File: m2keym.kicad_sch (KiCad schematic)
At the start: 14 parts, among them J6 Bus_M.2_1-2199230-6

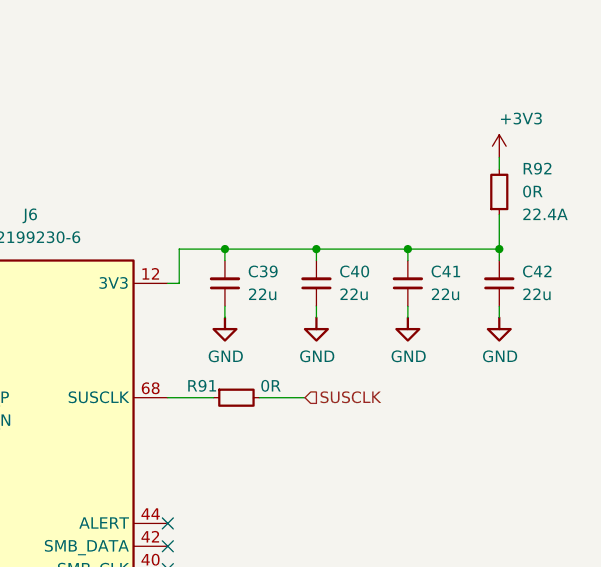
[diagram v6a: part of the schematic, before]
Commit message: [#58137] Add DC/DC supplies
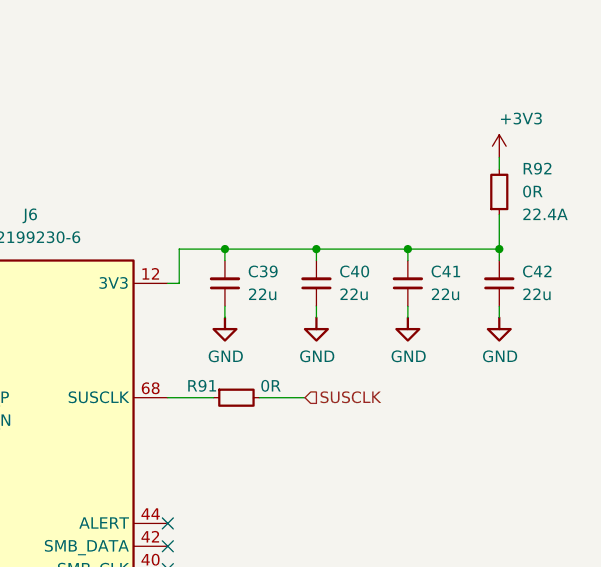
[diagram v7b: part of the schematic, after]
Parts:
- C39, C40, C41, C42: value C_22u_0603 -> C_22u_16V_0603; symbol antmicroCapacitors0603:C_22u_0603 -> antmicroCapacitors0603:C_22u_16V_0603; MPN GRM188R60J226MEA0D -> CL10A226MO7JZNC; Manufacturer Murata -> Samsung Electro-Mechanics; Voltage (none) -> 16V
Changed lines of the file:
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@@
     )
   )
-  (symbol (lib_id "antmicroCapacitors0603:C_22u_0603") (at 267.97 91.44 90) (unit 1)
+  (symbol (lib_id "antmicroCapacitors0603:C_22u_16V_0603") (at 267.97 91.44 90) (unit 1)
     (in_bom yes) (on_board yes) (dnp no) (fields_autoplaced)
-    (property "Reference" "C42" (at 270.51 87.6236 90)
-      (effects (font (size 1.27 1.27) (thickness 0.15)) (justify right))
-    )
-    (property "Value" "C_22u_0603" (at 278.13 71.12 0)
+    (property "Reference" "C42" (at 270.51 87.6235 90)
+      (effects (font (size 1.27 1.27) (thickness 0.15)) (justify right))
+    )
+    (property "Value" "C_22u_16V_0603" (at 278.13 71.12 0)
       (effects (font (size 1.27 1.27) (thickness 0.15)) (justify left bottom) hide)
     )
@@
       (effects (font (size 1.27 1.27) (thickness 0.15)) (justify left bottom) hide)
     )
-    (property "Datasheet" "https://www.murata.com/products/productdetail?partno=GRM188R60J226MEA0%23" (at 283.21 71.12 0)
-      (effects (font (size 1.27 1.27) (thickness 0.15)) (justify left bottom) hide)
-    )
-    (property "MPN" "GRM188R60J226MEA0D" (at 285.75 71.12 0)
-      (effects (font (size 1.27 1.27) (thickness 0.15)) (justify left bottom) hide)
-    )
-    (property "Manufacturer" "Murata" (at 288.29 71.12 0)
+    (property "Datasheet" "https://product.samsungsem.com/mlcc/CL10A226MO7JZN.do" (at 283.21 71.12 0)
+      (effects (font (size 1.27 1.27) (thickness 0.15)) (justify left bottom) hide)
+    )
+    (property "MPN" "CL10A226MO7JZNC" (at 285.75 71.12 0)
+      (effects (font (size 1.27 1.27) (thickness 0.15)) (justify left bottom) hide)
+    )
+    (property "Manufacturer" "Samsung Electro-Mechanics" (at 288.29 71.12 0)
       (effects (font (size 1.27 1.27) (thickness 0.15)) (justify left bottom) hide)
     )
@@
       (effects (font (size 1.27 1.27) (thickness 0.15)) (justify left bottom) hide)
     )
-    (property "Val" "22u" (at 270.51 90.1636 90)
-      (effects (font (size 1.27 1.27) (thickness 0.15)) (justify right))
-    )
-    (property "Voltage" "" (at 295.91 71.12 0)
+    (property "Val" "22u" (at 270.51 90.1635 90)
+      (effects (font (size 1.27 1.27) (thickness 0.15)) (justify right))
+    )
+    (property "Voltage" "16V" (at 295.91 71.12 0)
       (effects (font (size 1.27 1.27)) (justify left bottom) hide)
     )
@@
     )
   )
-  (symbol (lib_id "antmicroCapacitors0603:C_22u_0603") (at 257.81 91.44 90) (unit 1)
+  (symbol (lib_id "antmicroCapacitors0603:C_22u_16V_0603") (at 257.81 91.44 90) (unit 1)
     (in_bom yes) (on_board yes) (dnp no) (fields_autoplaced)
-    (property "Reference" "C41" (at 260.35 87.6236 90)
-      (effects (font (size 1.27 1.27) (thickness 0.15)) (justify right))
-    )
-    (property "Value" "C_22u_0603" (at 267.97 71.12 0)
+    (property "Reference" "C41" (at 260.35 87.6235 90)
+      (effects (font (size 1.27 1.27) (thickness 0.15)) (justify right))
+    )
+    (property "Value" "C_22u_16V_0603" (at 267.97 71.12 0)
       (effects (font (size 1.27 1.27) (thickness 0.15)) (justify left bottom) hide)
     )
@@
       (effects (font (size 1.27 1.27) (thickness 0.15)) (justify left bottom) hide)
     )
-    (property "Datasheet" "https://www.murata.com/products/productdetail?partno=GRM188R60J226MEA0%23" (at 273.05 71.12 0)
-      (effects (font (size 1.27 1.27) (thickness 0.15)) (justify left bottom) hide)
-    )
-    (property "MPN" "GRM188R60J226MEA0D" (at 275.59 71.12 0)
-      (effects (font (size 1.27 1.27) (thickness 0.15)) (justify left bottom) hide)
-    )
-    (property "Manufacturer" "Murata" (at 278.13 71.12 0)
+    (property "Datasheet" "https://product.samsungsem.com/mlcc/CL10A226MO7JZN.do" (at 273.05 71.12 0)
+      (effects (font (size 1.27 1.27) (thickness 0.15)) (justify left bottom) hide)
+    )
+    (property "MPN" "CL10A226MO7JZNC" (at 275.59 71.12 0)
+      (effects (font (size 1.27 1.27) (thickness 0.15)) (justify left bottom) hide)
+    )
+    (property "Manufacturer" "Samsung Electro-Mechanics" (at 278.13 71.12 0)
       (effects (font (size 1.27 1.27) (thickness 0.15)) (justify left bottom) hide)
     )
@@
       (effects (font (size 1.27 1.27) (thickness 0.15)) (justify left bottom) hide)
     )
-    (property "Val" "22u" (at 260.35 90.1636 90)
-      (effects (font (size 1.27 1.27) (thickness 0.15)) (justify right))
-    )
-    (property "Voltage" "" (at 285.75 71.12 0)
+    (property "Val" "22u" (at 260.35 90.1635 90)
+      (effects (font (size 1.27 1.27) (thickness 0.15)) (justify right))
+    )
+    (property "Voltage" "16V" (at 285.75 71.12 0)
       (effects (font (size 1.27 1.27)) (justify left bottom) hide)
     )
@@
     )
   )
-  (symbol (lib_id "antmicroCapacitors0603:C_22u_0603") (at 247.65 91.44 90) (unit 1)
+  (symbol (lib_id "antmicroCapacitors0603:C_22u_16V_0603") (at 247.65 91.44 90) (unit 1)
     (in_bom yes) (on_board yes) (dnp no) (fields_autoplaced)
-    (property "Reference" "C40" (at 250.19 87.6236 90)
-      (effects (font (size 1.27 1.27) (thickness 0.15)) (justify right))
-    )
-    (property "Value" "C_22u_0603" (at 257.81 71.12 0)
+    (property "Reference" "C40" (at 250.19 87.6235 90)
+      (effects (font (size 1.27 1.27) (thickness 0.15)) (justify right))
+    )
+    (property "Value" "C_22u_16V_0603" (at 257.81 71.12 0)
       (effects (font (size 1.27 1.27) (thickness 0.15)) (justify left bottom) hide)
     )
@@
       (effects (font (size 1.27 1.27) (thickness 0.15)) (justify left bottom) hide)
     )
-    (property "Datasheet" "https://www.murata.com/products/productdetail?partno=GRM188R60J226MEA0%23" (at 262.89 71.12 0)
-      (effects (font (size 1.27 1.27) (thickness 0.15)) (justify left bottom) hide)
-    )
-    (property "MPN" "GRM188R60J226MEA0D" (at 265.43 71.12 0)
-      (effects (font (size 1.27 1.27) (thickness 0.15)) (justify left bottom) hide)
-    )
-    (property "Manufacturer" "Murata" (at 267.97 71.12 0)
+    (property "Datasheet" "https://product.samsungsem.com/mlcc/CL10A226MO7JZN.do" (at 262.89 71.12 0)
+      (effects (font (size 1.27 1.27) (thickness 0.15)) (justify left bottom) hide)
+    )
+    (property "MPN" "CL10A226MO7JZNC" (at 265.43 71.12 0)
+      (effects (font (size 1.27 1.27) (thickness 0.15)) (justify left bottom) hide)
+    )
+    (property "Manufacturer" "Samsung Electro-Mechanics" (at 267.97 71.12 0)
       (effects (font (size 1.27 1.27) (thickness 0.15)) (justify left bottom) hide)
     )
@@
       (effects (font (size 1.27 1.27) (thickness 0.15)) (justify left bottom) hide)
     )
-    (property "Val" "22u" (at 250.19 90.1636 90)
-      (effects (font (size 1.27 1.27) (thickness 0.15)) (justify right))
-    )
-    (property "Voltage" "" (at 275.59 71.12 0)
+    (property "Val" "22u" (at 250.19 90.1635 90)
+      (effects (font (size 1.27 1.27) (thickness 0.15)) (justify right))
+    )
+    (property "Voltage" "16V" (at 275.59 71.12 0)
       (effects (font (size 1.27 1.27)) (justify left bottom) hide)
     )
@@
     )
   )
-  (symbol (lib_id "antmicroCapacitors0603:C_22u_0603") (at 237.49 91.44 90) (unit 1)
+  (symbol (lib_id "antmicroCapacitors0603:C_22u_16V_0603") (at 237.49 91.44 90) (unit 1)
     (in_bom yes) (on_board yes) (dnp no) (fields_autoplaced)
-    (property "Reference" "C39" (at 240.03 87.6236 90)
-      (effects (font (size 1.27 1.27) (thickness 0.15)) (justify right))
-    )
-    (property "Value" "C_22u_0603" (at 247.65 71.12 0)
+    (property "Reference" "C39" (at 240.03 87.6235 90)
+      (effects (font (size 1.27 1.27) (thickness 0.15)) (justify right))
+    )
+    (property "Value" "C_22u_16V_0603" (at 247.65 71.12 0)
       (effects (font (size 1.27 1.27) (thickness 0.15)) (justify left bottom) hide)
     )
@@
       (effects (font (size 1.27 1.27) (thickness 0.15)) (justify left bottom) hide)
     )
-    (property "Datasheet" "https://www.murata.com/products/productdetail?partno=GRM188R60J226MEA0%23" (at 252.73 71.12 0)
-      (effects (font (size 1.27 1.27) (thickness 0.15)) (justify left bottom) hide)
-    )
-    (property "MPN" "GRM188R60J226MEA0D" (at 255.27 71.12 0)
-      (effects (font (size 1.27 1.27) (thickness 0.15)) (justify left bottom) hide)
-    )
-    (property "Manufacturer" "Murata" (at 257.81 71.12 0)
+    (property "Datasheet" "https://product.samsungsem.com/mlcc/CL10A226MO7JZN.do" (at 252.73 71.12 0)
+      (effects (font (size 1.27 1.27) (thickness 0.15)) (justify left bottom) hide)
+    )
+    (property "MPN" "CL10A226MO7JZNC" (at 255.27 71.12 0)
+      (effects (font (size 1.27 1.27) (thickness 0.15)) (justify left bottom) hide)
+    )
+    (property "Manufacturer" "Samsung Electro-Mechanics" (at 257.81 71.12 0)
       (effects (font (size 1.27 1.27) (thickness 0.15)) (justify left bottom) hide)
     )
@@
       (effects (font (size 1.27 1.27) (thickness 0.15)) (justify left bottom) hide)
     )
-    (property "Val" "22u" (at 240.03 90.1636 90)
-      (effects (font (size 1.27 1.27) (thickness 0.15)) (justify right))
-    )
-    (property "Voltage" "" (at 265.43 71.12 0)
-      (effects (font (size 1.27 1.27)) (justify left bottom) hide)
-    )
+    (property "Val" "22u" (at 240.03 90.1635 90)
+      (effects (font (size 1.27 1.27) (thickness 0.15)) (justify right))
+    )
+    (property "Voltage" "16V" (at 265.43 71.12 0)
+      (effects (font (size 1.27 1.27)) (justify left bottom) hide)
+    )

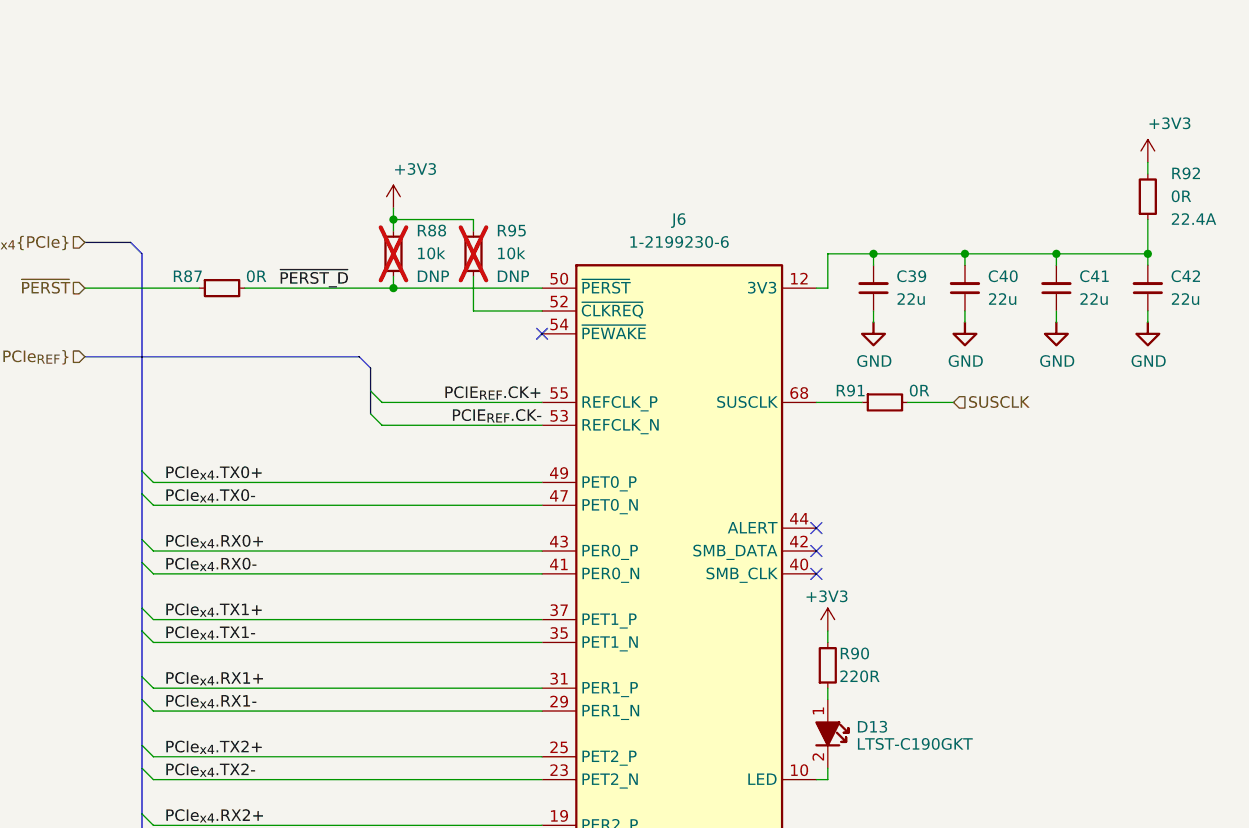
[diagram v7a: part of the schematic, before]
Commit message: Reannotate schematic
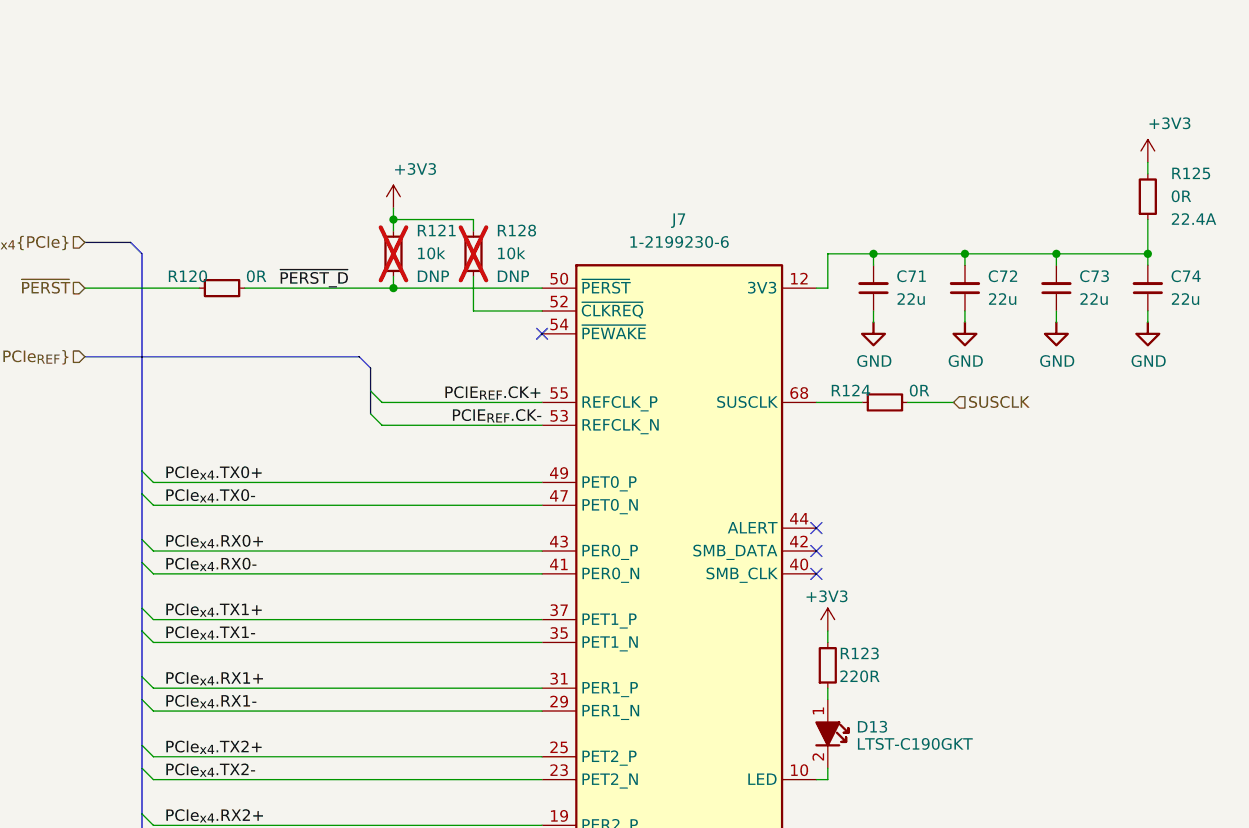
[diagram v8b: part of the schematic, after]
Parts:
- renumbered C39 to C71, C40 to C72, C41 to C73, C42 to C74, J6 to J7, R87 to R120, R88 to R121, R90 to R123, R91 to R124, R92 to R125, R95 to R128
